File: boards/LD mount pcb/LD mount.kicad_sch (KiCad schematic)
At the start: 5 parts

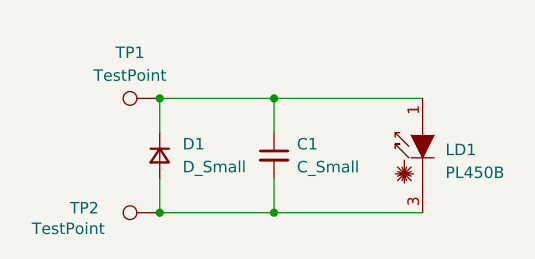
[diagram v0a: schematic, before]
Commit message: updated physical scanning chassis
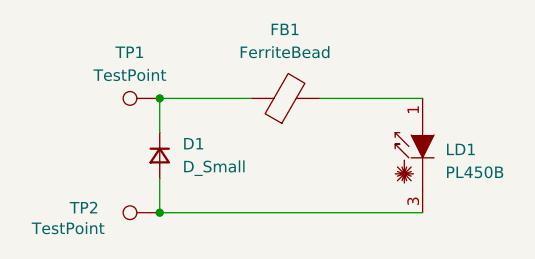
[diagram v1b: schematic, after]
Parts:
- removed C1: C_Small, Capacitor_SMD:C_0603_1608Metric_Pad1.08x0.95mm_HandSolder, symbol Device:C_Small
- added FB1: FerriteBead, Inductor_SMD:L_0603_1608Metric_Pad1.05x0.95mm_HandSolder, symbol Device:FerriteBead
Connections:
- net at D1.1 (K), TP1.1: now also FB1.1; no longer LD1.1 (A)
- new net: FB1.2, LD1.1 (A)
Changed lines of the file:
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@@
 	(paper "A4")
 	(junction
-		(at 121.92 127)
+		(at 121.92 114.3)
 		(diameter 0)
 		(color 0 0 0 0)
 	)
 	(junction
-		(at 134.62 114.3)
-		(diameter 0)
-		(color 0 0 0 0)
-	)
-	(junction
-		(at 134.62 127)
-		(diameter 0)
-		(color 0 0 0 0)
-	)
-	(junction
-		(at 121.92 114.3)
+		(at 121.92 127)
 		(diameter 0)
 		(color 0 0 0 0)
@@
 	(wire
 		(pts
-			(xy 134.62 123.19) (xy 134.62 127)
+			(xy 121.92 127) (xy 151.13 127)
 		)
 		(stroke
@@
 	(wire
 		(pts
-			(xy 134.62 127) (xy 151.13 127)
+			(xy 121.92 114.3) (xy 132.08 114.3)
 		)
 		(stroke
@@
 	(wire
 		(pts
-			(xy 134.62 118.11) (xy 134.62 114.3)
-		)
-		(stroke
-			(width 0)
-			(type default)
-		)
-	)
-	(wire
-		(pts
-			(xy 134.62 127) (xy 121.92 127)
-		)
-		(stroke
-			(width 0)
-			(type default)
-		)
-	)
-	(wire
-		(pts
-			(xy 134.62 114.3) (xy 121.92 114.3)
-		)
-		(stroke
-			(width 0)
-			(type default)
-		)
-	)
-	(wire
-		(pts
-			(xy 134.62 114.3) (xy 151.13 114.3)
+			(xy 139.7 114.3) (xy 151.13 114.3)
 		)
 		(stroke
@@
 	)
 	(symbol
-		(lib_id "Device:C_Small")
-		(at 134.62 120.65 0)
+		(lib_id "Device:FerriteBead")
+		(at 135.89 114.3 90)
 		(unit 1)
 		(exclude_from_sim no)
@@
 		(dnp no)
 		(fields_autoplaced yes)
-		(property "Reference" "C1"
-			(at 137.16 119.3862 0)
+		(property "Reference" "FB1"
+			(at 135.8392 106.68 90)
 			(effects
 				(font
 					(size 1.27 1.27)
 				)
-				(justify left)
 			)
 		)
-		(property "Value" "C_Small"
-			(at 137.16 121.9262 0)
+		(property "Value" "FerriteBead"
+			(at 135.8392 109.22 90)
 			(effects
 				(font
 					(size 1.27 1.27)
 				)
-				(justify left)
 			)
 		)
-		(property "Footprint" "Capacitor_SMD:C_0603_1608Metric_Pad1.08x0.95mm_HandSolder"
-			(at 134.62 120.65 0)
+		(property "Footprint" "Inductor_SMD:L_0603_1608Metric_Pad1.05x0.95mm_HandSolder"
+			(at 135.89 116.078 90)
 			(effects
 				(font
@@
 		)
 		(property "Datasheet" "~"
-			(at 134.62 120.65 0)
+			(at 135.89 114.3 0)
 			(effects
 				(font
@@
 			)
 		)
-		(property "Description" "Unpolarized capacitor, small symbol"
-			(at 134.62 120.65 0)
+		(property "Description" "Ferrite bead"
+			(at 135.89 114.3 0)
 			(effects
 				(font
@@
 			)
 		)
+		(pin "2"
+		)
 		(pin "1"
-		)
-		(pin "2"
 		)
 		(instances
 			(project "LD mount"
 				(path "/08b3d1a9-1627-471f-a392-fd1d4e3923e4"
-					(reference "C1")
+					(reference "FB1")
 					(unit 1)
 				)
